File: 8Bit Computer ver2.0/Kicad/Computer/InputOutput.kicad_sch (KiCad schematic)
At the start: 56 parts, among them IC232 SN74ABT245BDWR, IC233 SN74AHC540DWR, IC234 SN74ABT574ADWR, IC235 SN74ABT245BDWR, IC236 SN74F521DWR, IC237 SN74LVC1G14DBVR, IC238 SN74LVC1G08DBVR, IC239 SN74AHC74DR, IC240 SN74LVC1G14DBVR, IC241 SN74AHC74DR, IC242 SN74AHC74DR, IC243 SN74LVC1G14DBVR, IC244 SN74F521DWR, IC245 SN74LVC1G14DBVR, IC246 SN74ABT245BDWR, IC247 SN74F521DWR, IC248 SN74ABT574ADWR, IC249 SN74LVC1G14DBVR, IC250 SN74F521DWR, IC251 SN74LVC1G14DBVR, IC252 SN74LVC1G08DBVR, IC253 SN74AHC74DR, IC254 SN74LVC1G14DBVR, IC255 SN74AHC540DWR

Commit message: Kicad, parts
parts:
added Flipswitch
added Inductor for PSU
added Step-Down Conv chip MP2338GTL
Kicad:
added Step-Down Conv circuit for 20V VBUS to 5V VCC
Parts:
- added C121, C127: 0.1uF, Capacitor_SMD:C_1206_3216Metric_Pad1.33x1.80mm_HandSolder, symbol Device:C
- added C122, C123, C126: 22uF, Capacitor_SMD:C_1206_3216Metric_Pad1.33x1.80mm_HandSolder, symbol Device:C
- added C125: 22nF, Capacitor_SMD:C_1206_3216Metric_Pad1.33x1.80mm_HandSolder, symbol Device:C
- added C128: 300pF, Capacitor_SMD:C_1206_3216Metric_Pad1.33x1.80mm_HandSolder, symbol Device:C
- added IC256: MP2338GTL-Z, Samacsys:MP2338GTLZ, symbol Samacsys:MP2338GTL-Z
- added L1: 6.8uH, Samacsys:INDPM108100X400N, symbol Device:L
- added R28, R29, R30: 10k, Resistor_SMD:R_1206_3216Metric_Pad1.30x1.75mm_HandSolder, symbol Device:R
- added R32: 49.9k, Resistor_SMD:R_1206_3216Metric_Pad1.30x1.75mm_HandSolder, symbol Device:R
- added R33: 191k, Resistor_SMD:R_1206_3216Metric_Pad1.30x1.75mm_HandSolder, symbol Device:R
- added R34: 90.9k, Resistor_SMD:R_1206_3216Metric_Pad1.30x1.75mm_HandSolder, symbol Device:R
- added S1, S2, S3, S4, S5, S6, S7, S8: 2MS1T2B3M2QES, Samacsys:2MS1T2B3M2QES, symbol Samacsys:2MS1T2B3M2QES
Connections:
- net GND: now also C122.2, C123.2, C125.2, C126.1, C127.1, IC256.4 (GND), R30.2, R32.2, S1.3 (NC), S2.3 (NC), S3.3 (NC), S4.3 (NC), S5.3 (NC), S6.3 (NC), S7.3 (NC), S8.3 (NC)
- net INBval0: now also S1.2 (COM)
- net INBval1: now also S2.2 (COM)
- net INBval2: now also S3.2 (COM)
- net INBval3: now also S4.2 (COM)
- net INBval4: now also S5.2 (COM)
- net INBval5: now also S6.2 (COM)
- net INBval6: now also S7.2 (COM)
- net INBval7: now also S8.2 (COM)
- net VCC: now also C122.1, C123.1, C128.1, L1.1, R28.1, R34.2, S1.1 (NO), S2.1 (NO), S3.1 (NO), S4.1 (NO), S5.1 (NO), S6.1 (NO), S7.1 (NO), S8.1 (NO)
- new net: C128.2, R29.2, R30.1, R34.1
- new net: C125.1, IC256.7 (SS)
- new net: IC256.1 (PG), R28.2
- new net: C121.1, IC256.3 (SW), L1.2
- new net: C121.2, IC256.5 (BST)
- new net: IC256.6 (EN), R32.1, R33.1
- new net: IC256.8 (FB), R29.1
- new net VBUS: C126.2, C127.2, IC256.2 (VIN), R33.2
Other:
- note added: "Switches"
- note removed: "Add switches"
- moved on the sheet: IC233, LED1, LED2, LED3, LED4, LED5, LED6, LED7, LED8, R12, R13, R14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

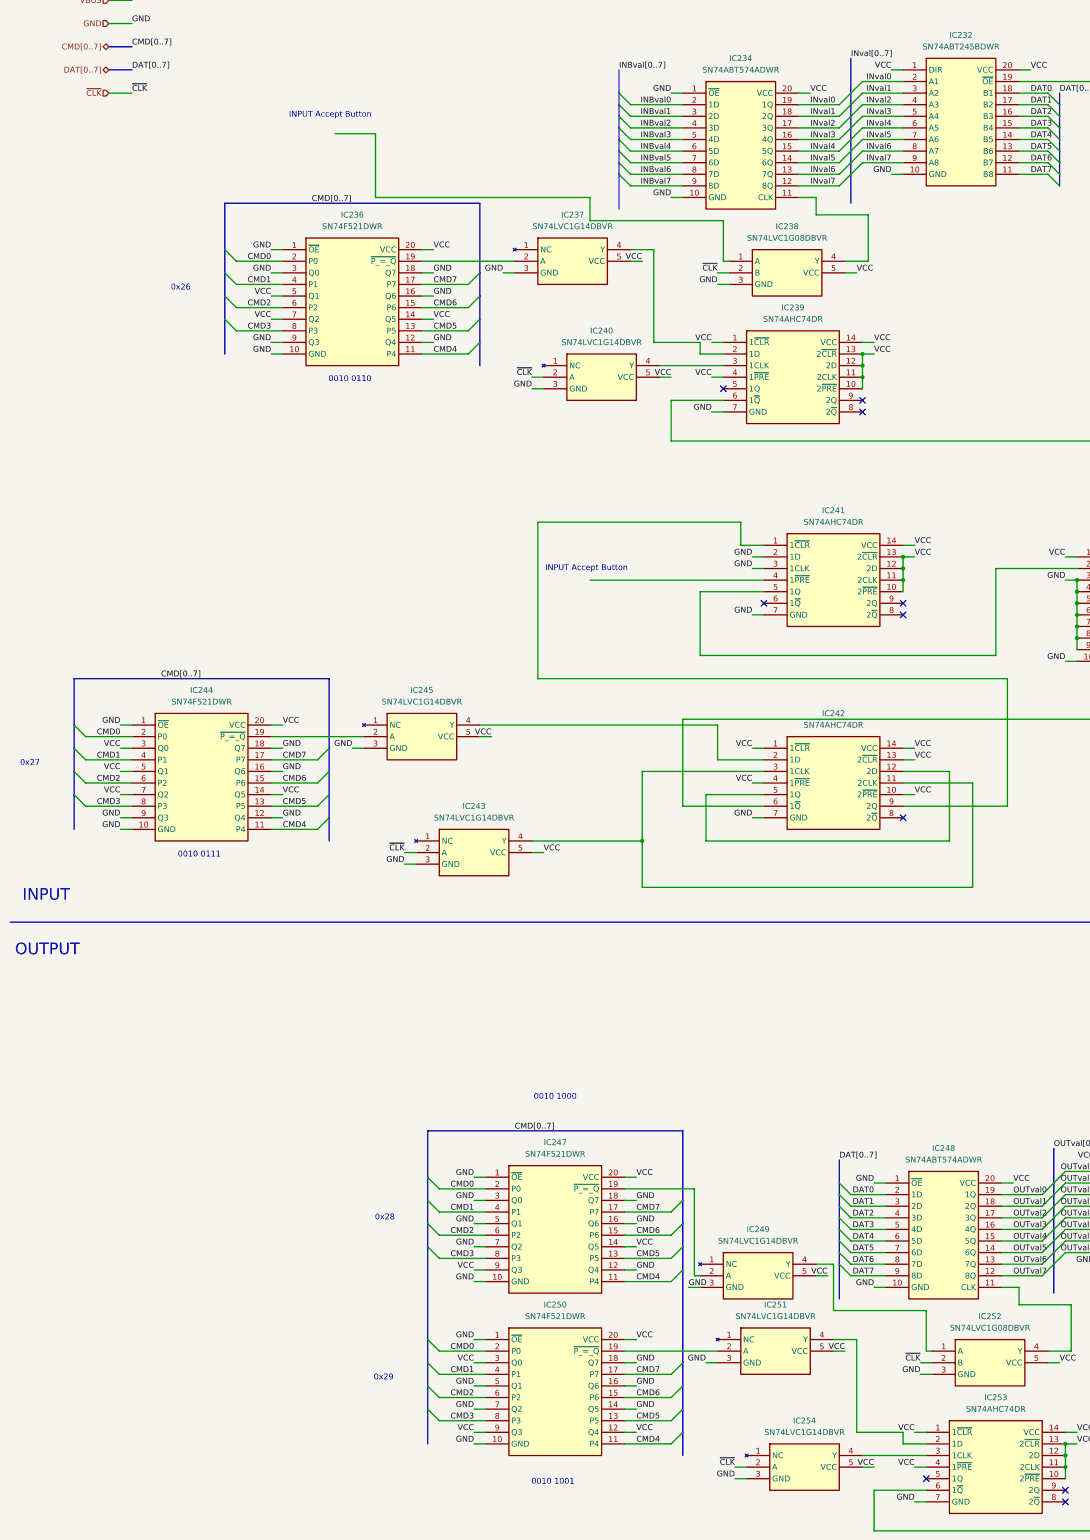
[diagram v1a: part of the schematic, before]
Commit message: Kicad, parts
parts:
added USB C PD Triggerboard
added Delay Chip for 90ns
added Push Button
Kicad:
added USB C PD Triggerboard
added rising edge detector via Delay and Xor for Accept Push Button
added VBUS net
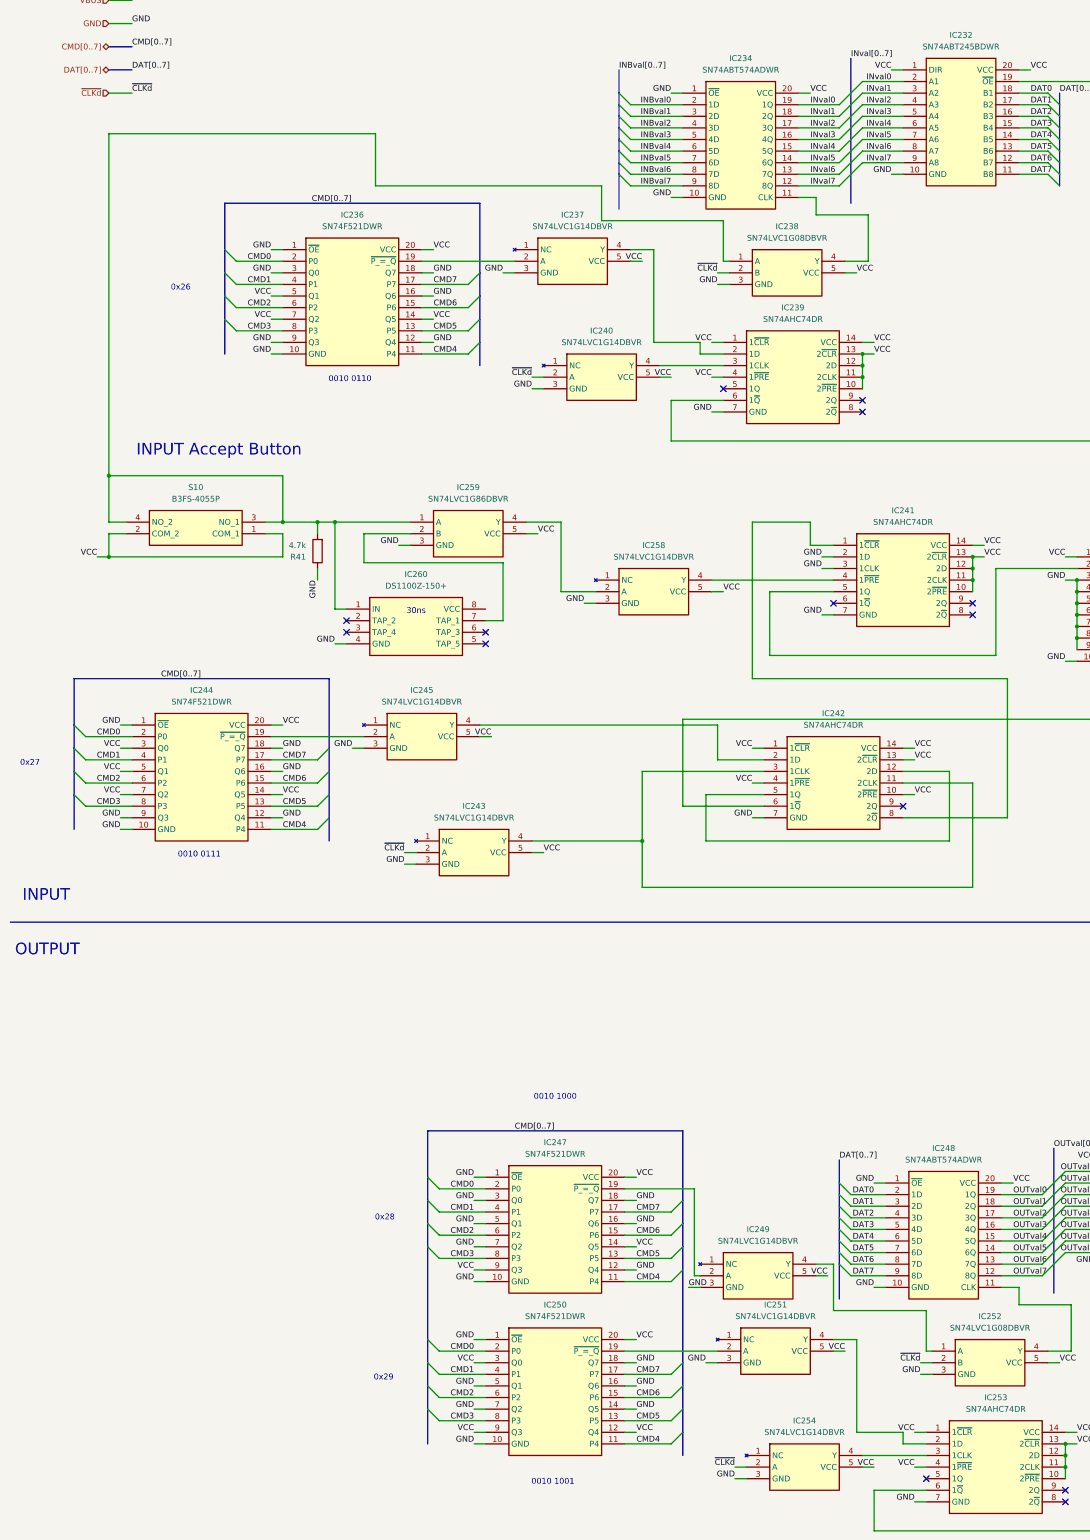
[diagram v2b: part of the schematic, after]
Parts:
- added IC258: SN74LVC1G14DBVR, Samacsys:SOT95P280X145-5N, symbol Samacsys:SN74LVC1G14DBVR
- added IC259: SN74LVC1G86DBVR, Samacsys:SOT95P280X145-5N, symbol Samacsys:SN74LVC1G86DBVR
- added IC260: DS1100Z-150+, Samacsys:SOIC127P600X175-8N, symbol Samacsys:DS1100Z-150+
- added R41: 4.7k, Resistor_SMD:R_1206_3216Metric_Pad1.30x1.75mm_HandSolder, symbol Device:R
- added S10: B3FS-4055P, Samacsys:B3FS4055P, symbol Samacsys:B3FS-4055P
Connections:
- net GND: now also IC258.3 (GND), IC259.3 (GND), IC260.4 (GND), R41.1
- net VCC: now also IC258.5 (VCC), IC259.5 (VCC), S10.1 (COM_1), S10.2 (COM_2)
- net at IC238.1 (A): now also IC259.1 (A), IC260.1 (IN), R41.2, S10.3 (NO_1), S10.4 (NO_2)
- net at IC242.8 (2~{Q}): now also IC241.1 (1~{CLR})
- net at IC242.9 (2Q): no longer IC241.1 (1~{CLR})
- net at IC241.4 (1~{PRE}): now also IC258.4 (Y)
- net ~{CLK} renamed ~{CLKd}
- new net: IC258.2 (A), IC259.4 (Y)
- new net: IC259.2 (B), IC260.7 (TAP_1)
- no-connect marks 10 -> 14
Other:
- note added: "30ns"
- moved on the sheet: IC241

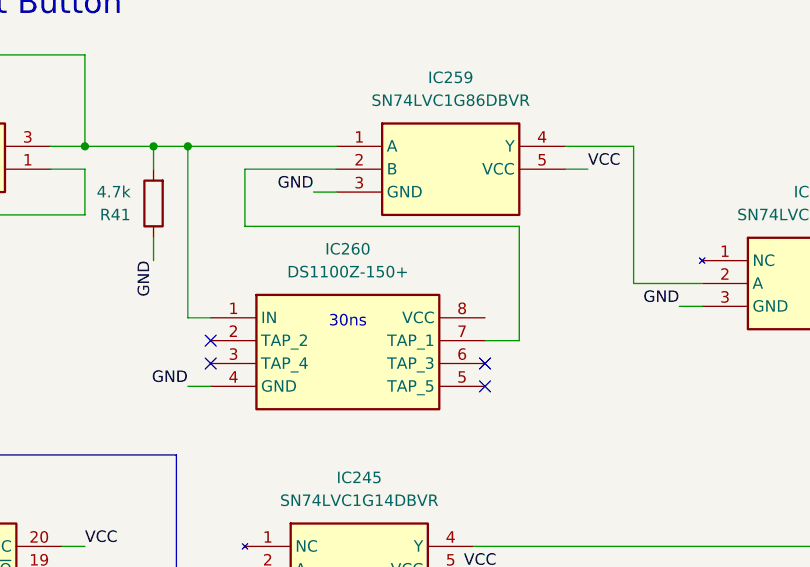
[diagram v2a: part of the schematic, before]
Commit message: Kicad
changed to module version
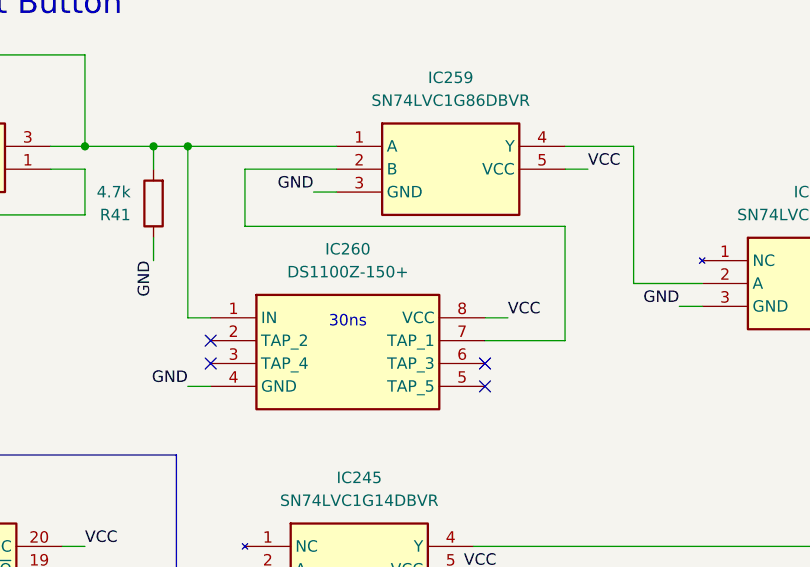
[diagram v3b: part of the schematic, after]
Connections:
- net VCC: now also IC260.8 (VCC)
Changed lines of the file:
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@@
 	(wire
 		(pts
-			(xy 120.65 185.42) (xy 124.46 185.42)
+			(xy 120.65 185.42) (xy 129.54 185.42)
 		)
 		(stroke
@@
 	(wire
 		(pts
-			(xy 124.46 172.72) (xy 93.98 172.72)
+			(xy 129.54 172.72) (xy 93.98 172.72)
 		)
 		(stroke
@@
 	(wire
 		(pts
+			(xy 120.65 182.88) (xy 123.19 182.88)
+		)
+		(stroke
+			(width 0)
+			(type default)
+		)
+	)
+	(wire
+		(pts
 			(xy 410.21 181.61) (xy 410.21 205.74)
 		)
@@
 	(wire
 		(pts
-			(xy 124.46 185.42) (xy 124.46 172.72)
+			(xy 129.54 185.42) (xy 129.54 172.72)
 		)
 		(stroke
@@
 		)
 	)
+	(label "VCC"
+		(at 123.19 182.88 0)
+		(effects
+			(font
+				(size 1.27 1.27)
+			)
+			(justify left bottom)
+		)
+	)

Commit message: Kicad SCH/PCB
Kicad SCH/PCB:
changed the References in SCH
began with INOUTPUT module nearly done
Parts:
- added C174, C181, C183, C184, C185, C186, C187, C188, C189, C190, C191, C192, C193, C194, C195, C196, C197, C198, C199, C200, C201, C202, C203, C204, C205, C206, C207, C208, C209, C210, C211, C212, C213, C214, C215, C216: 100nF, Capacitor_SMD:C_1206_3216Metric_Pad1.33x1.80mm_HandSolder, symbol Device:C
- added R35, R39, R42, R45, R50, R54, R57, R60: 4.7k, Resistor_SMD:R_1206_3216Metric_Pad1.30x1.75mm_HandSolder, symbol Device:R
- renumbered C122 to C175, C126 to C176, C123 to C177, C127 to C178, C121 to C179, C125 to C180, C128 to C182, IC244 to IC236, IC236 to IC237, IC260 to IC238, IC245 to IC239, IC259 to IC240, IC243 to IC241, IC247 to IC242, IC250 to IC243, IC237 to IC244, IC240 to IC245, IC258 to IC246, IC234 to IC247, IC249 to IC248, IC251 to IC249, IC239 to IC250, IC238 to IC251, IC254 to IC252, IC242 to IC253, IC241 to IC254, IC248 to IC255, IC232 to IC256, IC253 to IC257, IC252 to IC258, IC235 to IC259, IC246 to IC260, IC256 to IC261, IC255 to IC262, IC233 to IC263, L1 to L4, LED16 to LED1, LED5 to LED11, LED9 to LED12, LED4 to LED13, LED3 to LED14, LED2 to LED15, LED1 to LED16, LED15 to LED2, LED14 to LED3, LED13 to LED4, LED8 to LED5, LED12 to LED6, LED11 to LED8, LED6 to LED9, R41 to R31, R28 to R32, R32 to R34, R29 to R36, R34 to R37, R30 to R38, R27 to R40, R26 to R41, R25 to R43, R24 to R44, R18 to R46, R23 to R47, R19 to R48, R22 to R49, R16 to R51, R21 to R52, R17 to R53, R20 to R55, R14 to R56, R15 to R58, R13 to R59, R12 to R61, S1 to S10, S10 to S2, S8 to S3, S7 to S4, S6 to S5, S5 to S6, S4 to S7, S3 to S8, S2 to S9
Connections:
- net GND: now also C174.2, C181.1, C183.1, C184.1, C185.1, C186.1, C187.1, C188.1, C189.1, C190.1, C191.1, C192.1, C193.1, C194.1, C195.1, C196.1, C197.1, C198.1, C199.1, C200.1, C201.1, C202.1, C203.1, C204.1, C205.1, C206.1, C207.1, C208.1, C209.1, C210.1, C211.1, C212.1, C213.1, C214.1, C215.1, C216.1
- net INBval0: now also C189.2, R60.1; no longer S10.2 (COM)
- net INBval1: now also C188.2, R57.1; no longer S9.2 (COM)
- net INBval2: now also C187.2, R54.1; no longer S8.2 (COM)
- net INBval3: now also C186.2, R50.1; no longer S7.2 (COM)
- net INBval4: now also C185.2, R45.1; no longer S6.2 (COM)
- net INBval5: now also C184.2, R42.1; no longer S5.2 (COM)
- net INBval6: now also C183.2, R39.1; no longer S4.2 (COM)
- net INBval7: now also C181.2, R35.1; no longer S3.2 (COM)
- net OUTval0: now also IC262.9 (A8); no longer IC262.2 (A1)
- net OUTval1: now also IC262.8 (A7); no longer IC262.3 (A2)
- net OUTval2: now also IC262.7 (A6); no longer IC262.4 (A3)
- net OUTval3: now also IC262.6 (A5); no longer IC262.5 (A4)
- net OUTval4: now also IC262.5 (A4); no longer IC262.6 (A5)
- net OUTval5: now also IC262.4 (A3); no longer IC262.7 (A6)
- net OUTval6: now also IC262.3 (A2); no longer IC262.8 (A7)
- net OUTval7: now also IC262.2 (A1); no longer IC262.9 (A8)
- net VCC: now also LED1.2 (A), LED10.2 (A), LED12.2 (A), LED2.2 (A), LED3.2 (A), LED4.2 (A), LED6.2 (A), LED8.2 (A), C190.2, C191.2, C192.2, C193.2, C194.2, C195.2, C196.2, C197.2, C198.2, C199.2, C200.2, C201.2, C202.2, C203.2, C204.2, C205.2, C206.2, C207.2, C208.2, C209.2, C210.2, C211.2, C212.2, C213.2, C214.2, C215.2, C216.2; no longer R40.1, R41.1, R43.1, R44.1, R47.1, R49.1, R52.1, R55.1
- net at LED1.1 (K): now also R40.1; no longer IC262.11 (Y8)
- net at R40.2: now also IC262.11 (Y8); no longer LED1.2 (A)
- net at R52.2: now also IC262.17 (Y2); no longer LED10.2 (A)
- net at R41.2: now also IC262.12 (Y7); no longer LED2.2 (A)
- net at R43.2: now also IC262.13 (Y6); no longer LED3.2 (A)
- net at LED8.1 (K): now also R49.1; no longer IC262.16 (Y3)
- net at R49.2: now also IC262.16 (Y3); no longer LED8.2 (A)
- net at LED12.1 (K): now also R55.1; no longer IC262.18 (Y1)
- net at R55.2: now also IC262.18 (Y1); no longer LED12.2 (A)
- net at IC238.1 (IN), IC240.1 (A), IC251.1 (A)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: now also C174.1
- net at LED4.1 (K): now also R44.1; no longer IC262.14 (Y5)
- net at R44.2: now also IC262.14 (Y5); no longer LED4.2 (A)
- net at LED3.1 (K): now also R43.1; no longer IC262.13 (Y6)
- net at LED10.1 (K): now also R52.1; no longer IC262.17 (Y2)
- net at LED2.1 (K): now also R41.1; no longer IC262.12 (Y7)
- net at R47.2: now also IC262.15 (Y4); no longer LED6.2 (A)
- net at LED6.1 (K): now also R47.1; no longer IC262.15 (Y4)
- new net: R54.2, S8.2 (COM)
- new net: R42.2, S5.2 (COM)
- new net: R45.2, S6.2 (COM)
- new net: R60.2, S10.2 (COM)
- new net: R39.2, S4.2 (COM)
- new net: R57.2, S9.2 (COM)
- new net: R50.2, S7.2 (COM)
- new net: R35.2, S3.2 (COM)
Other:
- moved on the sheet: R40, R41, R43, R44, R47, R49, R52, R55

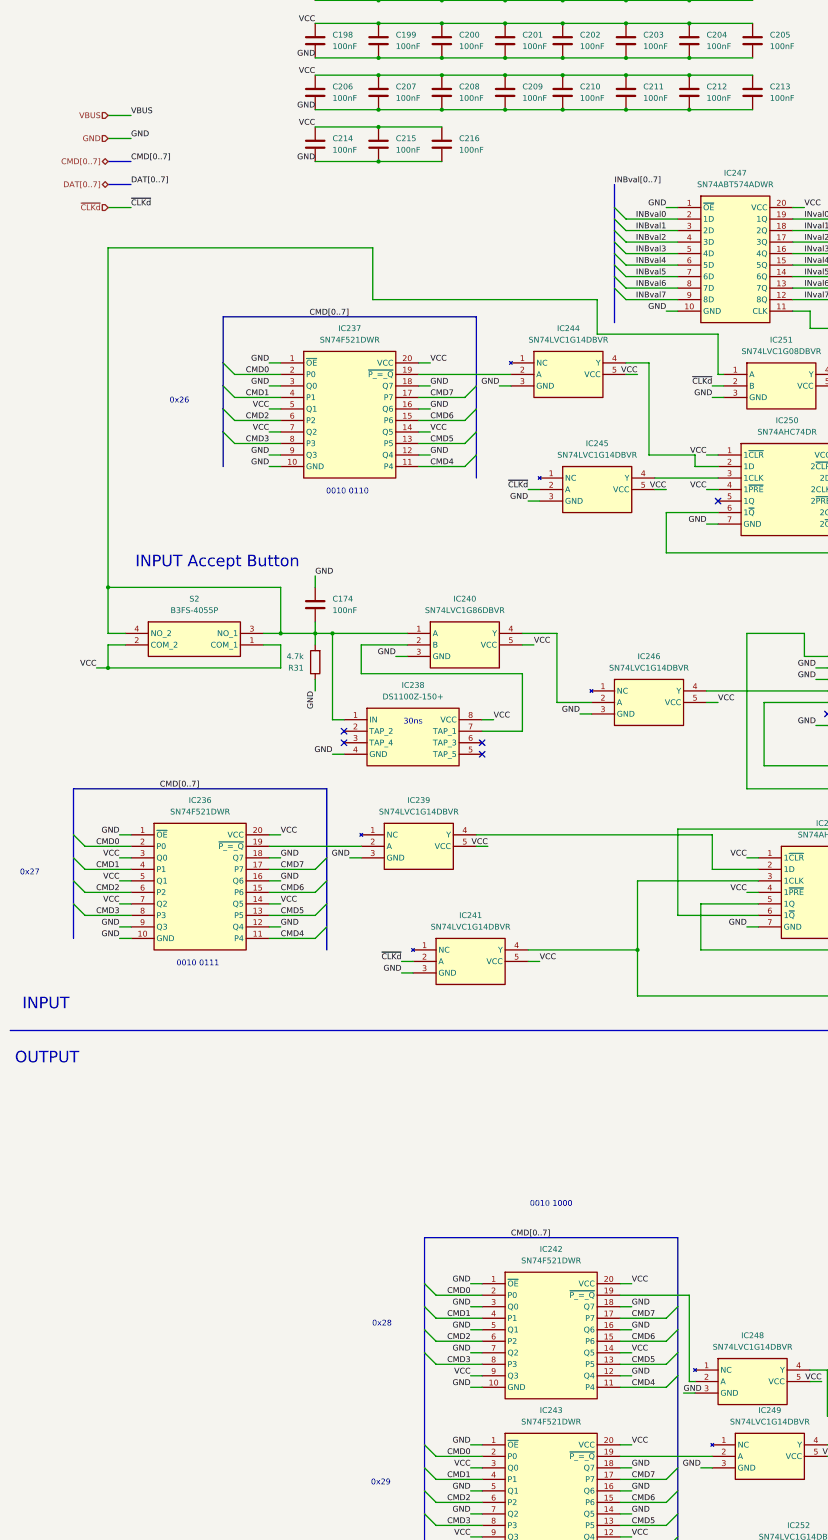
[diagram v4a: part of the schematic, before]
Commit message: Kicad, parts
parts:
added Mux 4:1 for CLK
added LM555
Kicad:
added some Diodes for Flash disable
fixed wrong routing of flag register
fixed wrong routing of STC STF in INC/AddS
LM555 circuit for 1Hz to 100Hz
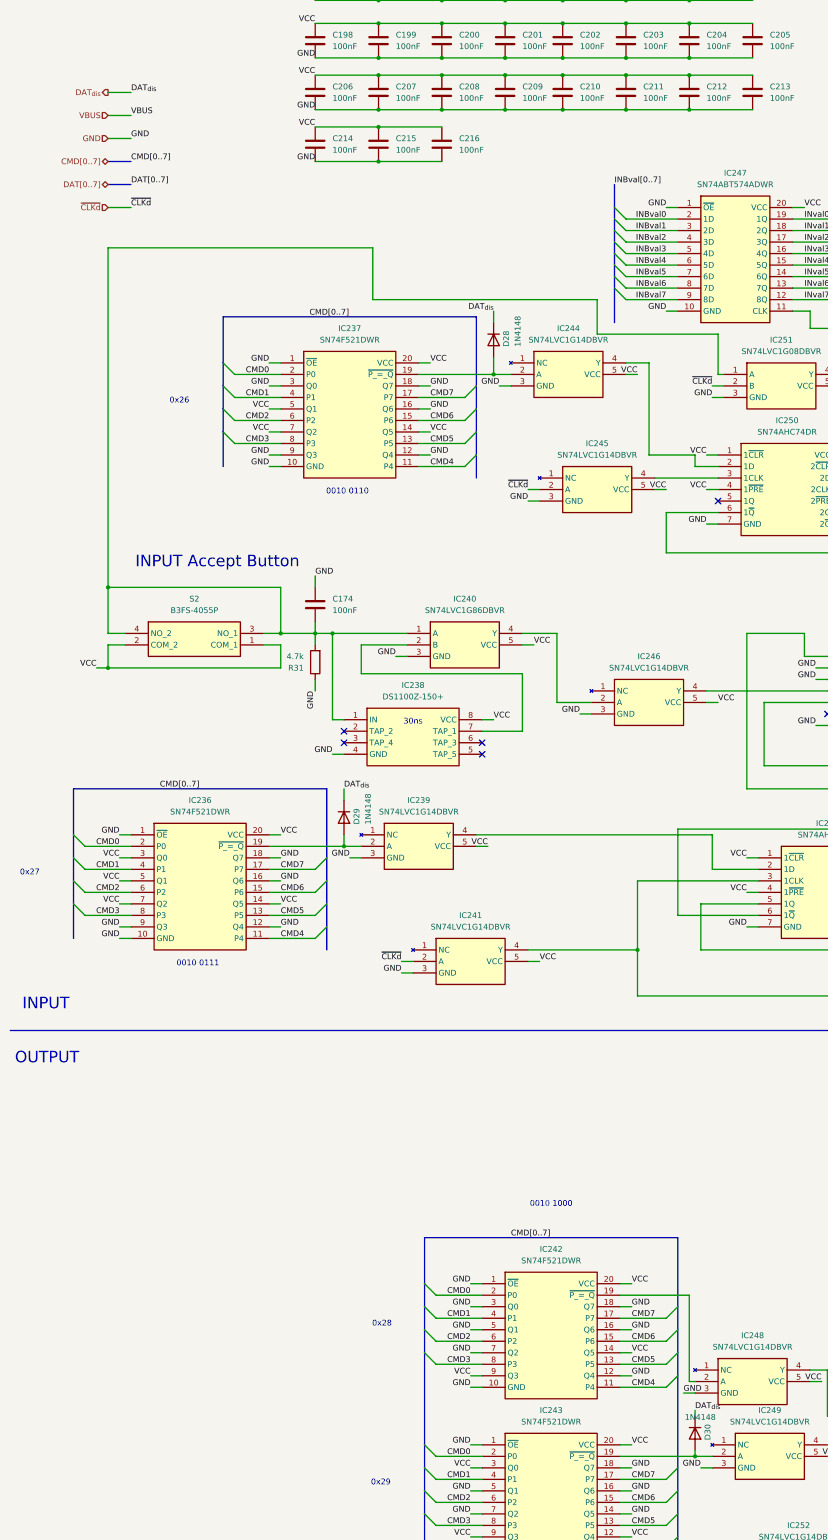
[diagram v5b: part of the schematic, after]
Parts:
- added D28, D29, D30: 1N4148, Diode_THT:D_DO-35_SOD27_P10.16mm_Horizontal, symbol Diode:1N4148
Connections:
- net at IC243.19 (~{P_=_Q}), IC249.2 (A): now also D30.2 (A)
- net at IC236.19 (~{P_=_Q}), IC239.2 (A): now also D29.2 (A)
- net at IC237.19 (~{P_=_Q}), IC244.2 (A): now also D28.2 (A)
- new net DAT_{dis}: D28.1 (K), D29.1 (K), D30.1 (K)
